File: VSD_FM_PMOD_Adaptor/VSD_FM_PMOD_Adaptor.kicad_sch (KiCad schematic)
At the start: 21 parts, among them J1 PMOD, J2 PMOD, U1 VSDSquadron FM, U2 AMS1117-3.3

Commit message: Updated LCSC component part numbers
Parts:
- C4: LCSC (none) -> C1713
- C5: LCSC (none) -> C380337
- D1, D2, D3, D4, D5, D6, D7, D8, J3: LCSC (none) -> C965799
- J1, J2: LCSC (none) -> IPCP254F12PB28R
- RN1, RN2, RN3, RN4: LCSC (none) -> C6332196
- RN5, RN6: LCSC (none) -> C309681
- U1: LCSC (none) -> C172477
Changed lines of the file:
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@@
 			)
 		)
-		(property "LCSC" ""
+		(property "LCSC" "C6332196"
 			(at 43.18 167.64 0)
 			(effects
@@
 			)
 		)
-		(property "LCSC" ""
+		(property "LCSC" "C309681"
 			(at 219.71 109.22 0)
 			(effects
@@
 			)
 		)
-		(property "LCSC" ""
+		(property "LCSC" "C965799"
 			(at 243.84 38.1 0)
 			(effects
@@
 			)
 		)
-		(property "LCSC" ""
+		(property "LCSC" "C6332196"
 			(at 43.18 172.72 0)
 			(effects
@@
 			)
 		)
-		(property "LCSC" ""
+		(property "LCSC" "C965799"
 			(at 240.03 116.84 0)
 			(effects
@@
 			)
 		)
-		(property "LCSC" ""
+		(property "LCSC" "C6332196"
 			(at 43.18 165.1 0)
 			(effects
@@
 			)
 		)
-		(property "LCSC" ""
+		(property "LCSC" "C6332196"
 			(at 43.18 127 0)
 			(effects
@@
 			)
 		)
-		(property "LCSC" ""
+		(property "LCSC" "IPCP254F12PB28R"
 			(at 74.93 127 0)
 			(effects
@@
 			)
 		)
-		(property "LCSC" ""
+		(property "LCSC" "C6332196"
 			(at 43.18 129.54 0)
 			(effects
@@
 			)
 		)
-		(property "LCSC" ""
+		(property "LCSC" "IPCP254F12PB28R"
 			(at 74.93 170.18 0)
 			(effects
@@
 			)
 		)
-		(property "LCSC" ""
+		(property "LCSC" "C6332196"
 			(at 43.18 124.46 0)
 			(effects
@@
 			)
 		)
-		(property "LCSC" ""
+		(property "LCSC" "C6332196"
 			(at 111.76 167.64 0)
 			(effects
@@
 			)
 		)
-		(property "LCSC" ""
+		(property "LCSC" "C309681"
 			(at 219.71 139.7 0)
 			(effects
@@
 			)
 		)
-		(property "LCSC" ""
+		(property "LCSC" "C172477"
 			(at 50.8 55.88 0)
 			(effects
@@
 			)
 		)
-		(property "LCSC" ""
+		(property "LCSC" "C380337"
 			(at 228.6 46.99 0)
 			(effects
@@
 			)
 		)
-		(property "LCSC" ""
+		(property "LCSC" "C6332196"
 			(at 43.18 121.92 0)
 			(effects
@@
 			)
 		)
-		(property "LCSC" ""
+		(property "LCSC" "C309681"
 			(at 219.71 147.32 0)
 			(effects
@@
 			)
 		)
-		(property "LCSC" ""
+		(property "LCSC" "C309681"
 			(at 219.71 144.78 0)
 			(effects
@@
 			)
 		)
-		(property "LCSC" ""
+		(property "LCSC" "C309681"
 			(at 219.71 114.3 0)
 			(effects
@@
 			)
 		)
-		(property "LCSC" ""
+		(property "LCSC" "C965799"
 			(at 240.03 139.7 0)
 			(effects
@@
 			)
 		)
-		(property "LCSC" ""
+		(property "LCSC" "C309681"
 			(at 219.71 116.84 0)
 			(effects
@@
 			)
 		)
-		(property "LCSC" ""
+		(property "LCSC" "C309681"
 			(at 219.71 111.76 0)
 			(effects
@@
 			)
 		)
-		(property "LCSC" ""
+		(property "LCSC" "C6332196"
 			(at 111.76 170.18 0)
 			(effects
@@
 			)
 		)
-		(property "LCSC" ""
+		(property "LCSC" "C965799"
 			(at 240.03 147.32 0)
 			(effects
@@
 			)
 		)
-		(property "LCSC" ""
+		(property "LCSC" "C172477"
 			(at 137.16 43.18 0)
 			(effects
@@
 			)
 		)
-		(property "LCSC" ""
+		(property "LCSC" "C965799"
 			(at 240.03 144.78 0)
 			(effects
@@
 			)
 		)
-		(property "LCSC" ""
+		(property "LCSC" "C965799"
 			(at 240.03 109.22 0)
 			(effects
@@
 			)
 		)
-		(property "LCSC" ""
+		(property "LCSC" "C6332196"
 			(at 110.49 124.46 0)
 			(effects
@@
 			)
 		)
-		(property "LCSC" ""
+		(property "LCSC" "C1713"
 			(at 195.58 45.72 0)
 			(effects
@@
 			)
 		)
-		(property "LCSC" ""
+		(property "LCSC" "C6332196"
 			(at 111.76 165.1 0)
 			(effects
@@
 			)
 		)
-		(property "LCSC" ""
+		(property "LCSC" "C965799"
 			(at 240.03 114.3 0)
 			(effects
@@
 			)
 		)
-		(property "LCSC" ""
+		(property "LCSC" "C6332196"
 			(at 43.18 170.18 0)
 			(effects
@@
 			)
 		)
-		(property "LCSC" ""
+		(property "LCSC" "C6332196"
 			(at 110.49 127 0)
 			(effects
@@
 			)
 		)
-		(property "LCSC" ""
+		(property "LCSC" "C309681"
 			(at 219.71 142.24 0)
 			(effects
@@
 			)
 		)
-		(property "LCSC" ""
+		(property "LCSC" "C6332196"
 			(at 110.49 121.92 0)
 			(effects
@@
 			)
 		)
-		(property "LCSC" ""
+		(property "LCSC" "C6332196"
 			(at 110.49 129.54 0)
 			(effects
@@
 			)
 		)
-		(property "LCSC" ""
+		(property "LCSC" "C6332196"
 			(at 111.76 172.72 0)
 			(effects
@@
 			)
 		)
-		(property "LCSC" ""
+		(property "LCSC" "C965799"
 			(at 240.03 111.76 0)
 			(effects
@@
 			)
 		)
-		(property "LCSC" ""
+		(property "LCSC" "C965799"
 			(at 240.03 142.24 0)
 			(effects

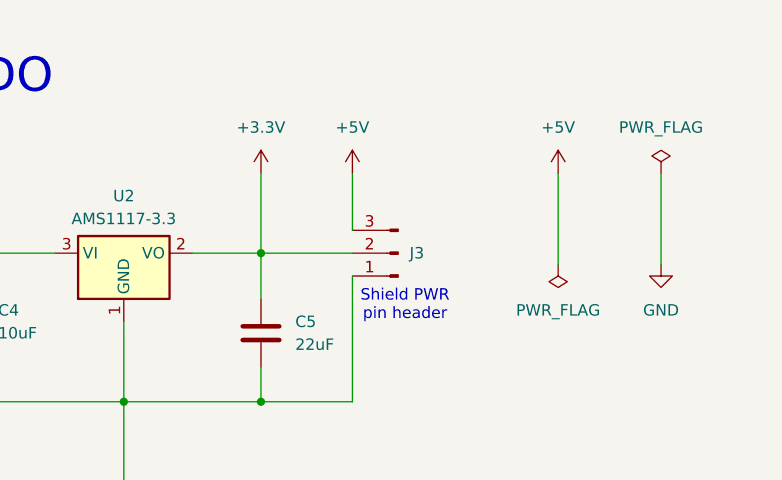
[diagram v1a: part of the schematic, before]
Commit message: Updated LCSC parts
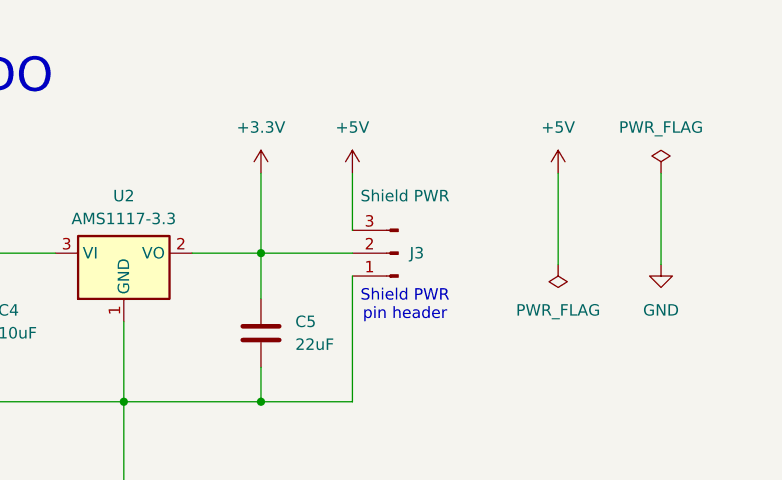
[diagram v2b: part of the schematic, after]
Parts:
- J1, J2: LCSC IPCP254F12PB28R -> C22438455
- J3: value ~ -> Shield PWR; LCSC C965799 -> C6332196
- RN1, RN2, RN3, RN4: LCSC C6332196 -> C309681
- RN5, RN6: LCSC C309681 -> C172477
- U1: LCSC C172477 -> (none)
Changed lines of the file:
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@@
 			)
 		)
-		(property "LCSC" "C6332196"
+		(property "LCSC" "C309681"
 			(at 43.18 167.64 0)
 			(effects
@@
 			)
 		)
-		(property "LCSC" "C309681"
+		(property "LCSC" "C172477"
 			(at 219.71 109.22 0)
 			(effects
@@
 		(on_board yes)
 		(dnp no)
-		(fields_autoplaced yes)
 		(property "Reference" "J3"
 			(at 245.11 38.0999 0)
@@
 			)
 		)
-		(property "Value" "~"
-			(at 243.205 43.18 0)
+		(property "Value" "Shield PWR"
+			(at 244.602 31.75 0)
 			(effects
 				(font
@@
 			)
 		)
-		(property "LCSC" "C965799"
+		(property "LCSC" "C6332196"
 			(at 243.84 38.1 0)
 			(effects
@@
 			)
 		)
-		(property "LCSC" "C6332196"
+		(property "LCSC" "C309681"
 			(at 43.18 172.72 0)
 			(effects
@@
 			)
 		)
-		(property "LCSC" "C6332196"
+		(property "LCSC" "C309681"
 			(at 43.18 165.1 0)
 			(effects
@@
 			)
 		)
-		(property "LCSC" "C6332196"
+		(property "LCSC" "C309681"
 			(at 43.18 127 0)
 			(effects
@@
 			)
 		)
-		(property "LCSC" "IPCP254F12PB28R"
+		(property "LCSC" "C22438455"
 			(at 74.93 127 0)
 			(effects
@@
 			)
 		)
-		(property "LCSC" "C6332196"
+		(property "LCSC" "C309681"
 			(at 43.18 129.54 0)
 			(effects
@@
 			)
 		)
-		(property "LCSC" "IPCP254F12PB28R"
+		(property "LCSC" "C22438455"
 			(at 74.93 170.18 0)
 			(effects
@@
 			)
 		)
-		(property "LCSC" "C6332196"
+		(property "LCSC" "C309681"
 			(at 43.18 124.46 0)
 			(effects
@@
 			)
 		)
-		(property "LCSC" "C6332196"
+		(property "LCSC" "C309681"
 			(at 111.76 167.64 0)
 			(effects
@@
 			)
 		)
-		(property "LCSC" "C309681"
+		(property "LCSC" "C172477"
 			(at 219.71 139.7 0)
 			(effects
@@
 			)
 		)
-		(property "LCSC" "C172477"
+		(property "LCSC" ""
 			(at 50.8 55.88 0)
 			(effects
@@
 			)
 		)
-		(property "LCSC" "C6332196"
+		(property "LCSC" "C309681"
 			(at 43.18 121.92 0)
 			(effects
@@
 			)
 		)
-		(property "LCSC" "C309681"
+		(property "LCSC" "C172477"
 			(at 219.71 147.32 0)
 			(effects
@@
 			)
 		)
-		(property "LCSC" "C309681"
+		(property "LCSC" "C172477"
 			(at 219.71 144.78 0)
 			(effects
@@
 			)
 		)
-		(property "LCSC" "C309681"
+		(property "LCSC" "C172477"
 			(at 219.71 114.3 0)
 			(effects
@@
 			)
 		)
-		(property "LCSC" "C309681"
+		(property "LCSC" "C172477"
 			(at 219.71 116.84 0)
 			(effects
@@
 			)
 		)
-		(property "LCSC" "C309681"
+		(property "LCSC" "C172477"
 			(at 219.71 111.76 0)
 			(effects
@@
 			)
 		)
-		(property "LCSC" "C6332196"
+		(property "LCSC" "C309681"
 			(at 111.76 170.18 0)
 			(effects
@@
 			)
 		)
-		(property "LCSC" "C172477"
+		(property "LCSC" ""
 			(at 137.16 43.18 0)
 			(effects
@@
 			)
 		)
-		(property "LCSC" "C6332196"
+		(property "LCSC" "C309681"
 			(at 110.49 124.46 0)
 			(effects
@@
 			)
 		)
-		(property "LCSC" "C6332196"
+		(property "LCSC" "C309681"
 			(at 111.76 165.1 0)
 			(effects
@@
 			)
 		)
-		(property "LCSC" "C6332196"
+		(property "LCSC" "C309681"
 			(at 43.18 170.18 0)
 			(effects
@@
 			)
 		)
-		(property "LCSC" "C6332196"
+		(property "LCSC" "C309681"
 			(at 110.49 127 0)
 			(effects
@@
 			)
 		)
-		(property "LCSC" "C309681"
+		(property "LCSC" "C172477"
 			(at 219.71 142.24 0)
 			(effects
@@
 			)
 		)
-		(property "LCSC" "C6332196"
+		(property "LCSC" "C309681"
 			(at 110.49 121.92 0)
 			(effects
@@
 			)
 		)
-		(property "LCSC" "C6332196"
+		(property "LCSC" "C309681"
 			(at 110.49 129.54 0)
 			(effects
@@
 			)
 		)
-		(property "LCSC" "C6332196"
+		(property "LCSC" "C309681"
 			(at 111.76 172.72 0)
 			(effects

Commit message: Adjust fill zones a bit
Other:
- company: VLSI System Design -> David Brough-Smyth
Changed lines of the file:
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@@
 	(title_block
 		(title "PMOD Adaptor for VSDSquadron FM Shield")
-		(date "2025-01-12")
+		(date "2025-01-25")
 		(rev "1A")
-		(company "VLSI System Design")
+		(company "David Brough-Smyth")
 	)
 	(junction
